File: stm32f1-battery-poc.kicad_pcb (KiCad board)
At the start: 4 copper layers, 92.5 x 85 mm, 153 parts, among them J1 Conn_01x02, J10 Conn_02x03_Odd_Even, J11 Conn_02x03_Odd_Even, J12 Conn_02x03_Odd_Even, J2 Conn_02x02_Odd_Even, J3 Conn_02x03_Odd_Even, J4 Conn_02x07_Odd_Even, J5 Conn_02x02_Odd_Even, J6 Conn_02x02_Odd_Even, J7 Conn_02x03_Odd_Even, J8 Conn_01x02, J9 Conn_01x04_Pin, M1 Stepper_Motor_bipolar, M2 Motor_3_Phases, Q1 Q_NMOS, Q2 Q_NMOS, SW1 SW_Push, SW2 SW_Push, SW3 SW_Push, SW4 SW_SPST, U1 LM78M05, U10 DRV8311H, U2 HT753-1, U3 SN65HVD230, U4 QRE1113GR, U5 QRE1113GR, U6 QRE1113GR, U7 DRV8424RGER, U8 STM32F103C8Tx, U9 BQ77905, Y1 8M

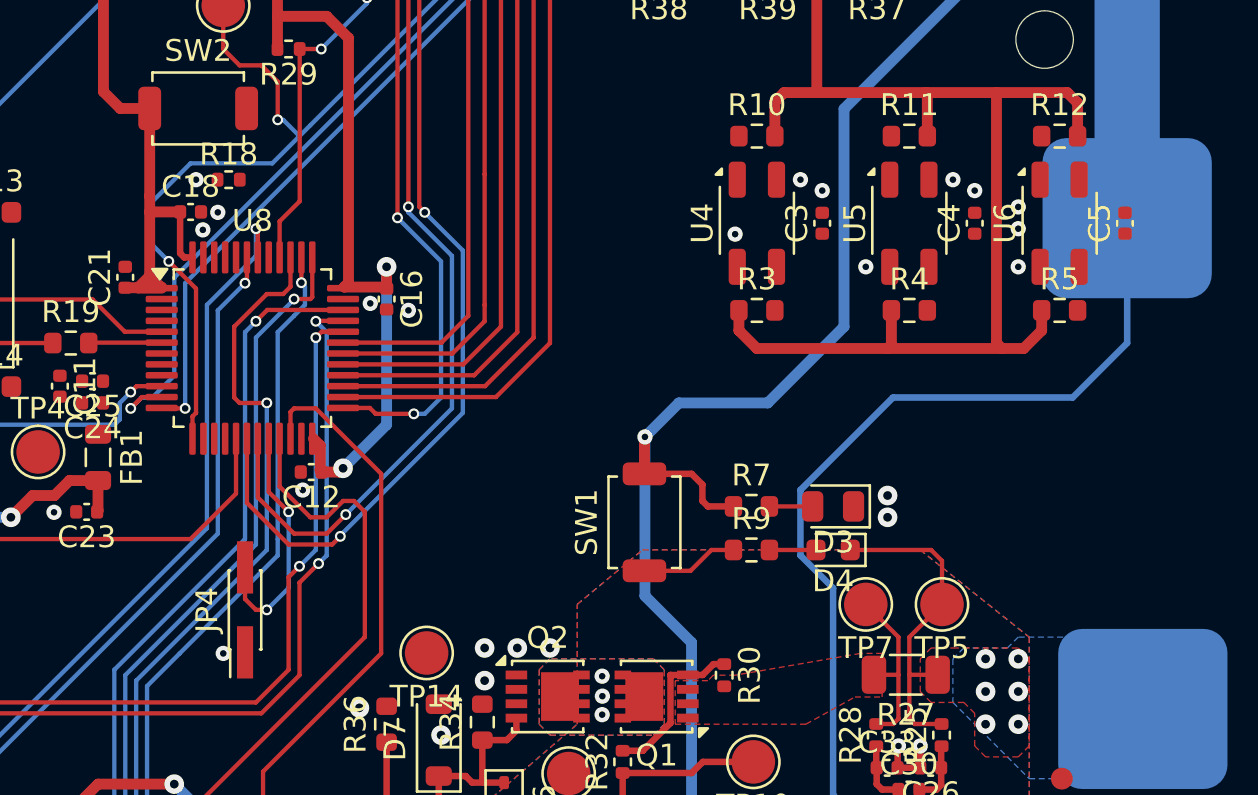
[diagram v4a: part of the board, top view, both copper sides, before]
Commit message: pcb: add QRE1113 routing
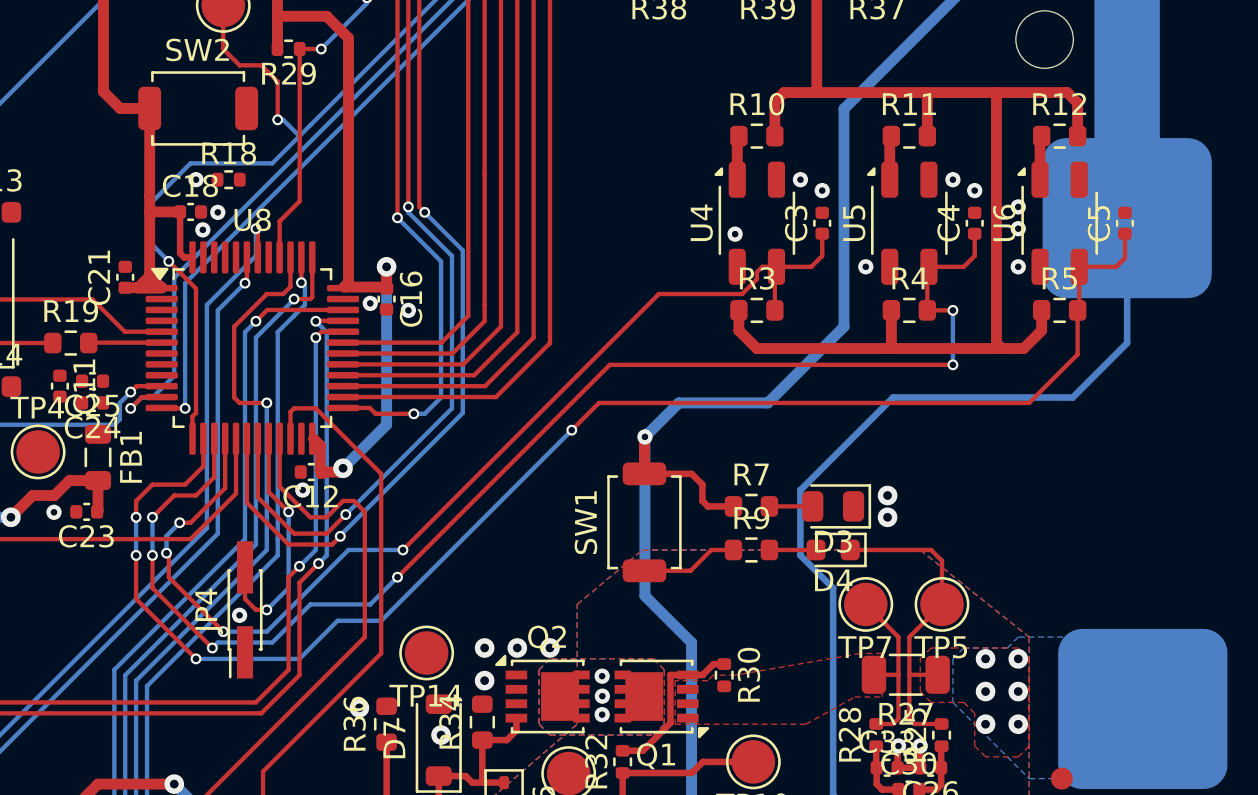
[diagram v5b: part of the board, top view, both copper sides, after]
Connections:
- U8 pad 14: /LS1 -> /LS3
- U8 pad 16: /LS3 -> /LS1
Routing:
- net /LS3: track 0.00 -> 67.1 mm, vias 0 -> 4
- net /LS2: track 0.00 -> 60.9 mm, vias 0 -> 6
- net /LS1: track 0.00 -> 49.2 mm, vias 0 -> 4
- net Net-(U5-A): track 0.00 -> 2.03 mm
- net Net-(U4-A): track 0.00 -> 2.03 mm
- net Net-(U6-A): track 0.00 -> 2.03 mm

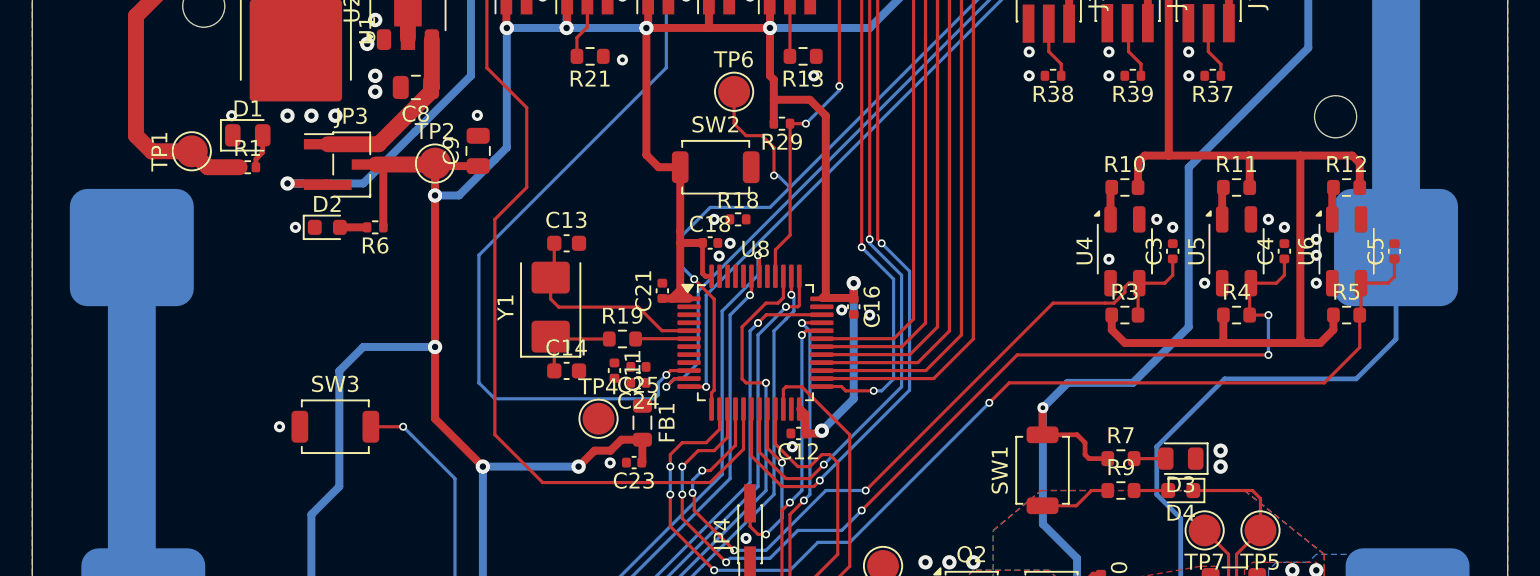
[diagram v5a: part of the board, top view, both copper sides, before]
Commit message: pcb: add NRST routing
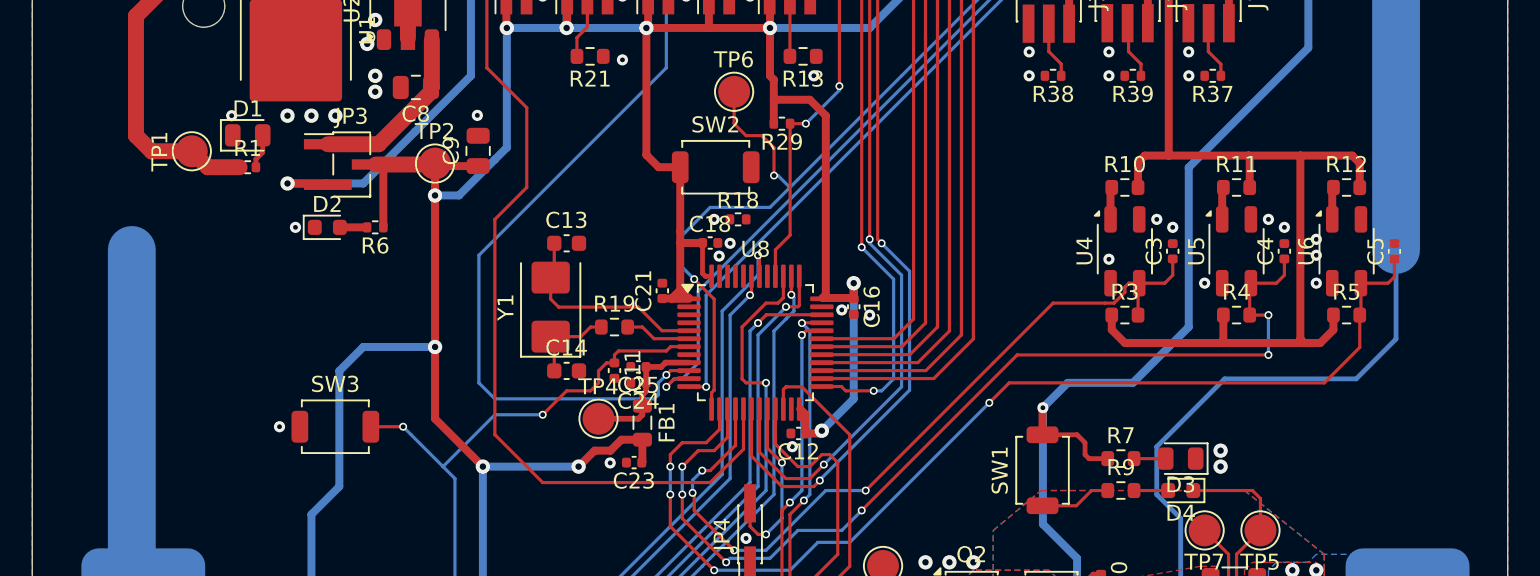
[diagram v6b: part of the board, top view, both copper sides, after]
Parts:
- removed BT2: Battery_Cell, GLCS:BatteryHolder_MYOUNG_BH-18650-B1BA002
- moved R19 0.90 mm to (139.0, 91.8)
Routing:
- net /NRST: track 34.7 -> 54.0 mm, vias 1 -> 2
- net Net-(U8-VDDA): track 0.00 -> 8.76 mm
- net /XTAL_O: track 3.36 -> 4.15 mm

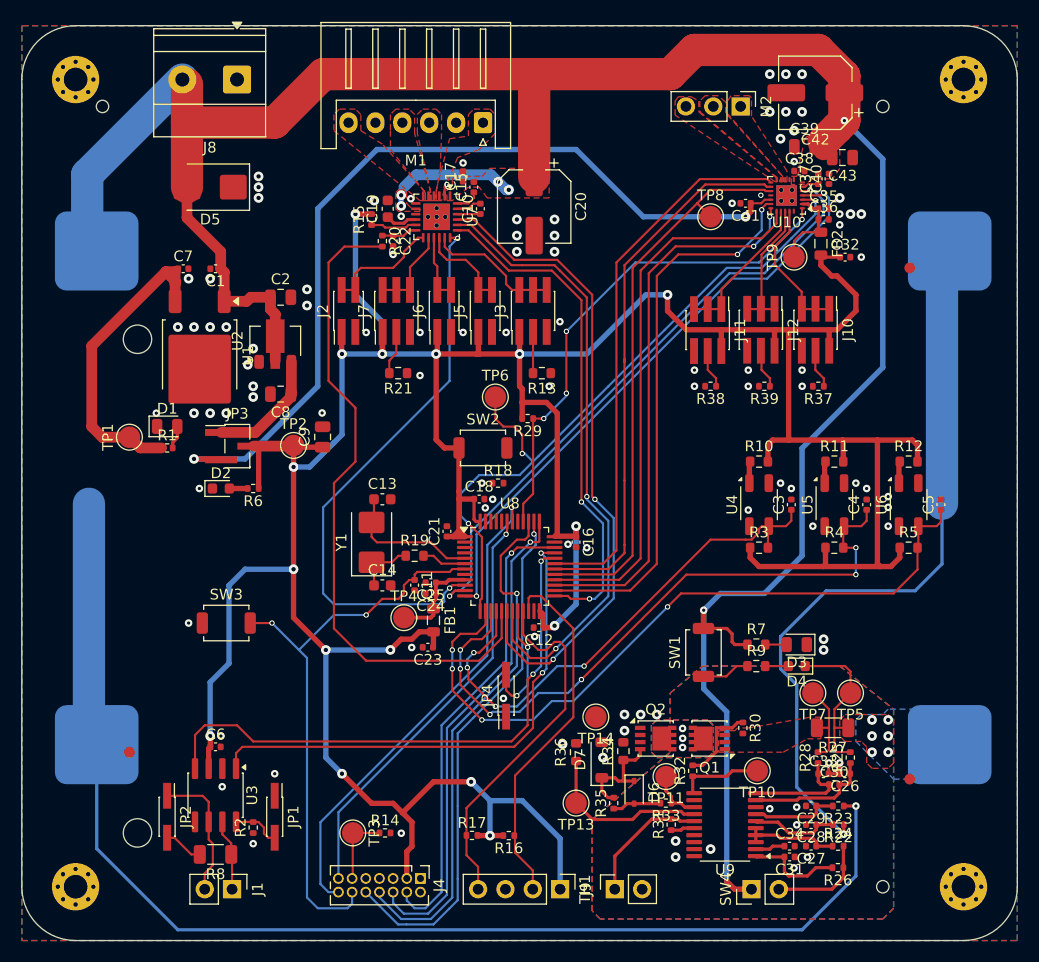
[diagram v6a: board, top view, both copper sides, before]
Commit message: pcb: add 5V routnig
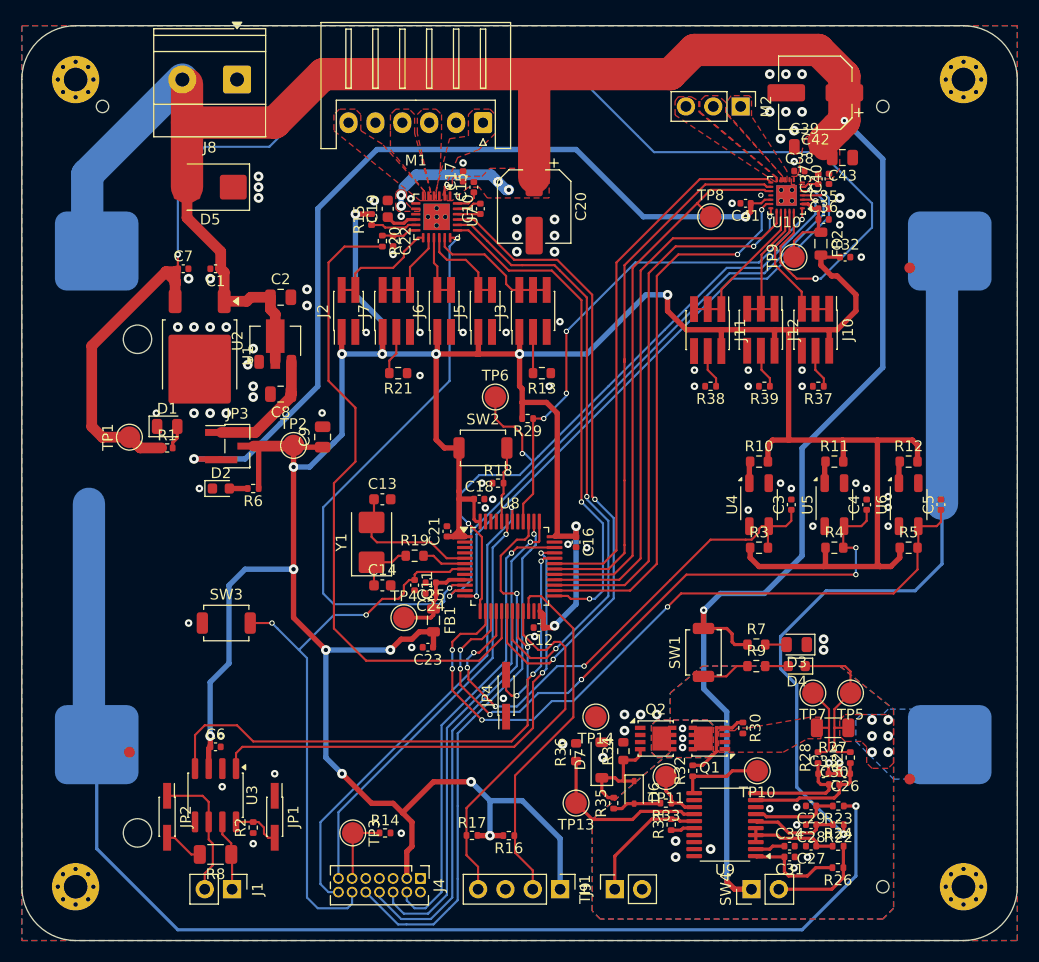
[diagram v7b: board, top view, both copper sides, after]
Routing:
- net +5V: track 30.1 -> 130.2 mm, vias 0 -> 2
- net /BOOT: track 0.00 -> 7.04 mm
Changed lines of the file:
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@@
+	)
+	(segment
+		(start 117 65.06)
+		(end 117.02 65.08)
+		(width 0.2)
+		(layer "F.Cu")
+		(net 10)
+	)
+	(segment
+		(start 172.999 64.518182)
+		(end 174.230818 65.75)
+		(width 0.2)
+		(layer "F.Cu")
+		(net 10)
 	)
 	(segment
@@
 	)
 	(segment
+		(start 174.23 59.73)
+		(end 174.23 61.77)
+		(width 0.2)
+		(layer "F.Cu")
+		(net 10)
+	)
+	(segment
 		(start 116.745 65.355)
 		(end 115.895 65.355)
@@
 	)
 	(segment
+		(start 173.25 62.75)
+		(end 172.999 63.001)
+		(width 0.2)
+		(layer "F.Cu")
+		(net 10)
+	)
+	(segment
 		(start 109 72.25)
 		(end 109 79.75)
@@
 	)
 	(segment
+		(start 174.230818 65.75)
+		(end 174.25 65.75)
+		(width 0.2)
+		(layer "F.Cu")
+		(net 10)
+	)
+	(segment
+		(start 174.23 61.77)
+		(end 173.25 62.75)
+		(width 0.2)
+		(layer "F.Cu")
+		(net 10)
+	)
+	(segment
 		(start 116.745 66.5)
 		(end 116.745 66.205)
@@
 	)
 	(segment
+		(start 174.25 65.75)
+		(end 174.5 66)
+		(width 0.2)
+		(layer "F.Cu")
+		(net 10)
+	)
+	(segment
+		(start 174.5 66)
+		(end 176.25 66)
+		(width 0.2)
+		(layer "F.Cu")
+		(net 10)
+	)
+	(segment
+		(start 172.999 63.001)
+		(end 172.999 64.518182)
+		(width 0.2)
+		(layer "F.Cu")
+		(net 10)
+	)
+	(segment
+		(start 117 63.75)
+		(end 117 65.06)
+		(width 0.2)
+		(layer "F.Cu")
+		(net 10)
+	)
+	(segment
 		(start 115.895 65.355)
 		(end 109 72.25)
 		(width 1)
 		(layer "F.Cu")
+		(net 10)
+	)
+	(via
+		(at 176.25 66)
+		(size 0.6)
+		(drill 0.3)
+		(layers "F.Cu" "B.Cu")
+		(net 10)
+	)
+	(via
+		(at 117 63.75)
+		(size 0.6)
+		(drill 0.3)
+		(layers "F.Cu" "B.Cu")
+		(net 10)
+	)
+	(segment
+		(start 179.75 63)
+		(end 181.5 61.25)
+		(width 0.2)
+		(layer "B.Cu")
+		(net 10)
+	)
+	(segment
+		(start 181.5 59)
+		(end 176.75 54.25)
+		(width 0.2)
+		(layer "B.Cu")
+		(net 10)
+	)
+	(segment
+		(start 181.5 61.25)
+		(end 181.5 59)
+		(width 0.2)
+		(layer "B.Cu")
+		(net 10)
+	)
+	(segment
+		(start 117 56.25)
+		(end 117 63.75)
+		(width 0.2)
+		(layer "B.Cu")
+		(net 10)
+	)
+	(segment
+		(start 126.75 52.5)
+		(end 125.5 53.75)
+		(width 0.2)
+		(layer "B.Cu")
+		(net 10)
+	)
+	(segment
+		(start 161.25 54.25)
+		(end 159.75 52.75)
+		(width 0.2)
+		(layer "B.Cu")
+		(net 10)
+	)
+	(segment
+		(start 131.5 47.75)
+		(end 126.75 52.5)
+		(width 0.2)
+		(layer "B.Cu")
+		(net 10)
+	)
+	(segment
+		(start 176.75 66)
+		(end 179.75 63)
+		(width 0.2)
+		(layer "B.Cu")
+		(net 10)
+	)
+	(segment
+		(start 125.5 53.75)
+		(end 119.5 53.75)
+		(width 0.2)
+		(layer "B.Cu")
+		(net 10)
+	)
+	(segment
+		(start 159.75 52.75)
+		(end 154.75 47.75)
+		(width 0.2)
+		(layer "B.Cu")
+		(net 10)
+	)
+	(segment
+		(start 144 47.75)
+		(end 131.5 47.75)
+		(width 0.2)
+		(layer "B.Cu")
+		(net 10)
+	)
+	(segment
+		(start 119.5 53.75)
+		(end 117 56.25)
+		(width 0.2)
+		(layer "B.Cu")
+		(net 10)
+	)
+	(segment
+		(start 176.75 54.25)
+		(end 176.25 54.25)
+		(width 0.2)
+		(layer "B.Cu")
+		(net 10)
+	)
+	(segment
+		(start 154.75 47.75)
+		(end 144 47.75)
+		(width 0.2)
+		(layer "B.Cu")
+		(net 10)
+	)
+	(segment
+		(start 176.25 66)
+		(end 176.75 66)
+		(width 0.2)
+		(layer "B.Cu")
+		(net 10)
+	)
+	(segment
+		(start 176.25 54.25)
+		(end 161.25 54.25)
+		(width 0.2)
+		(layer "B.Cu")
 		(net 10)
 	)
@@
 	)
 	(segment
+		(start 147.26 83.99)
+		(end 147.5725 83.6775)
+		(width 0.2)
+		(layer "F.Cu")
+		(net 80)
+	)
+	(segment
+		(start 147.5725 83.6775)
+		(end 147.5725 81.73)
+		(width 0.2)
+		(layer "F.Cu")
+		(net 80)
+	)
+	(segment
+		(start 147.26 85.99)
+		(end 147.0875 86.1625)
+		(width 0.2)
+		(layer "F.Cu")
+		(net 80)
+	)
+	(segment
+		(start 147.26 85)
+		(end 147.26 83.99)
+		(width 0.2)
+		(layer "F.Cu")
+		(net 80)
+	)
+	(segment
+		(start 147.0875 86.1625)
+		(end 147.0875 88.5675)
+		(width 0.2)
+		(layer "F.Cu")
+		(net 80)
+	)
+	(segment
+		(start 147.26 85)
+		(end 147.26 85.99)
+		(width 0.2)
+		(layer "F.Cu")
+		(net 80)
+	)
+	(segment
